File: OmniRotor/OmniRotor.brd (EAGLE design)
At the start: 118 parts, among them CON1 SPI, CON2 Telem, CON3 I2C, CON4 ADC, CON5 RC_IN, CON6 GPS, Q1 12MHz, U1 MAG3110, U2 LPS331AP, U3 HMC5883L, U4 BMP180, U6 XOR, U7 STM32F405RG, U8 LP2985-3.3, U9 LP2985-3.3

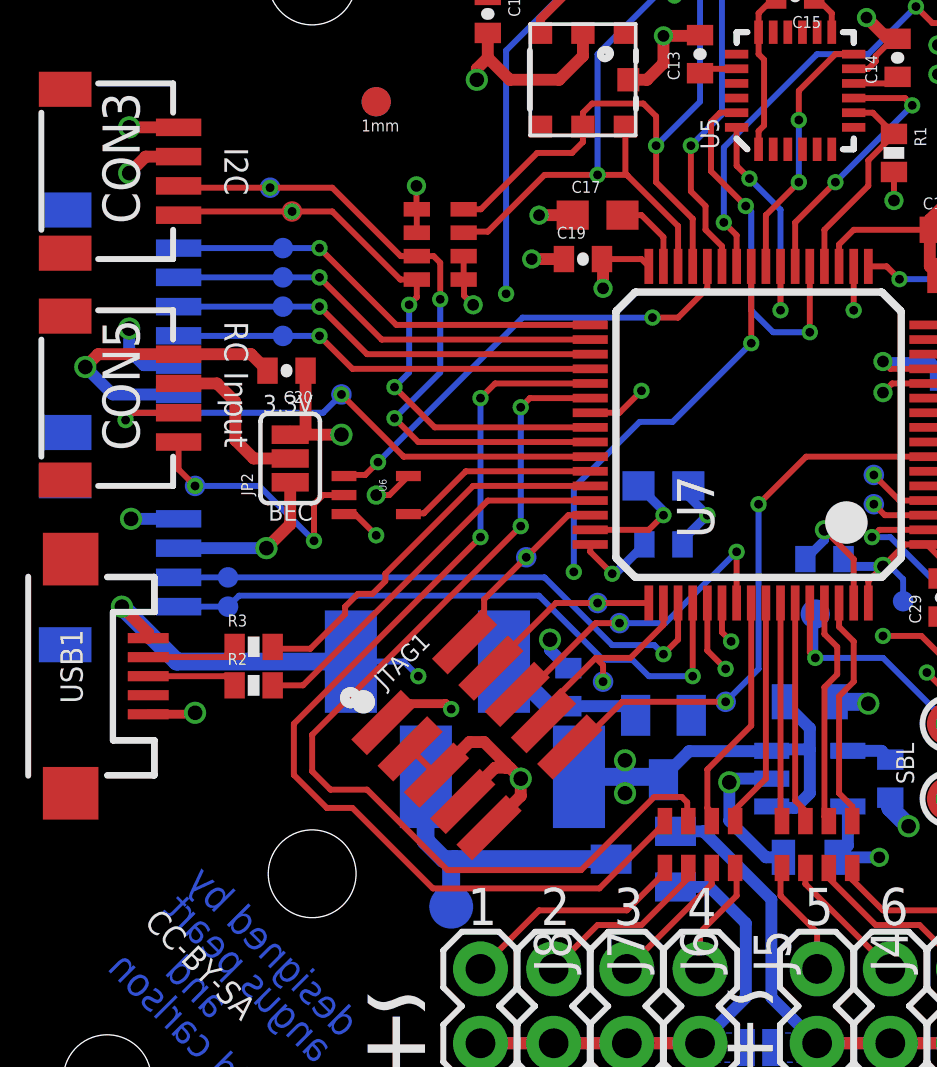
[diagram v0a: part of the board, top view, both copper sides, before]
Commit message: Changed debug interface from JTAG to SWD.
Frees up 2 GPIO. Also added pull-up and decoupling cap to reset line.
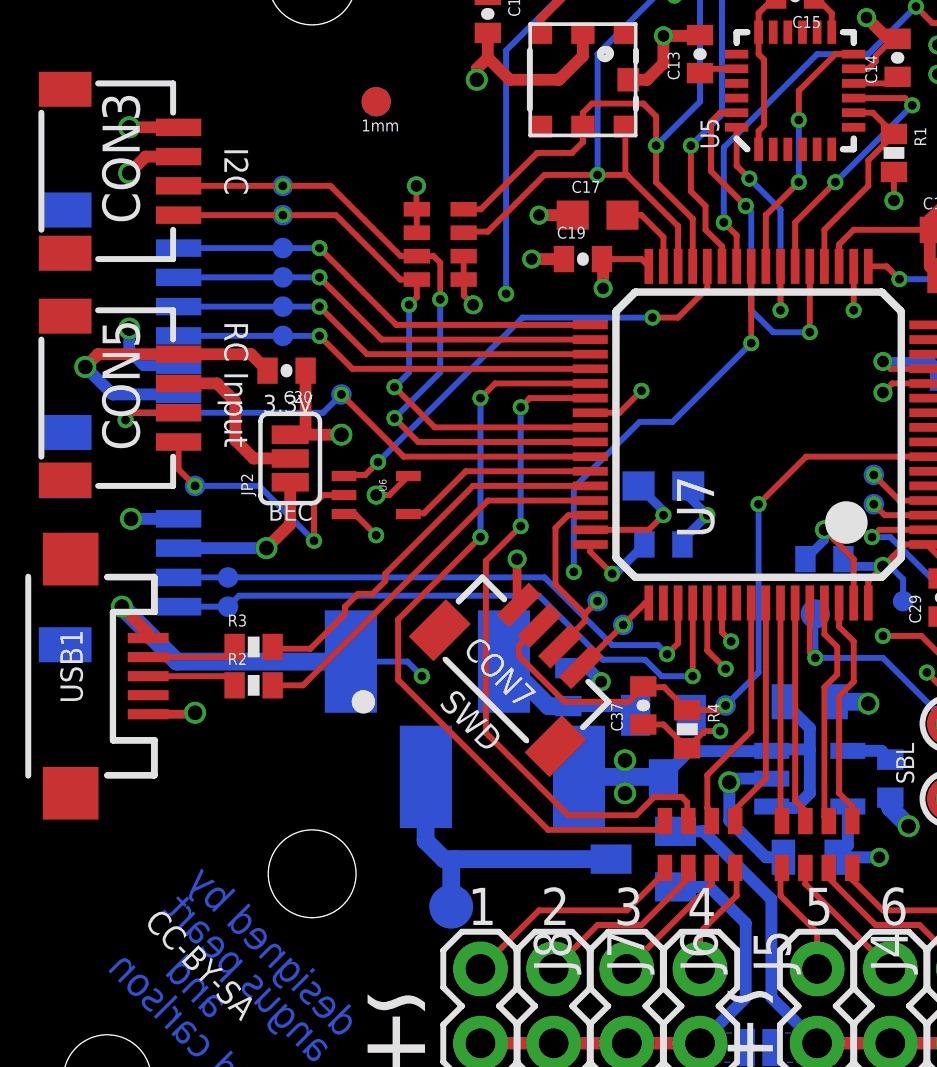
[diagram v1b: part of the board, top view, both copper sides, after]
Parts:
- removed JTAG1: (no value), OmniLoco:2X05-0.05IN
- removed TP21: TDO, OmniLoco:TESTPOINT_ROUND_0.7MM
- removed TP22: TDI, OmniLoco:TESTPOINT_ROUND_0.7MM
- added C37: 100nF, OmniLoco:0402-CAP
- added CON7: SWD, OmniLoco:BM04B-SRSS-TB
- added R4: 10K, OmniLoco:0402-RES
- TP19: value TMS -> SWDIO
- TP20: value TCLK -> SWDCLK
- TP23: value RST -> NRST
- moved TP19 2.86 mm to (19.5, 19.1)
- moved TP20 1.15 mm to (20.4, 18.2)
- moved TP9 0.44 mm to (8.75, 33.2)
- moved TP10 0.34 mm to (8.75, 32.2), flipped to the bottom
- moved TP23 0.12 mm to (23.9, 15.5)
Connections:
- removed net RST: JTAG1.10, TP23.1, U7.7
- removed net TCLK: JTAG1.4, TP20.1, U7.49
- removed net TDI: JTAG1.8, TP22.1, U7.50
- removed net TDO: JTAG1.6, TP21.1, U7.55
- removed net TMS: JTAG1.2, TP19.1, U7.46
- new net NRST: C37.2, CON7.2, R4.1, TP23.1, U7.7
- new net SWDCLK: CON7.4, TP20.1, U7.49
- new net SWDIO: CON7.3, TP19.1, U7.46
- net 3.3V: now also C37.1, R4.2; no longer JTAG1.1
- net GND: now also CON7.1; no longer JTAG1.3, JTAG1.5, JTAG1.7, JTAG1.9
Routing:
- net NRST: track 0.00 -> 23.5 mm, vias 0 -> 2
- net RST: track 19.6 -> 0.00 mm, vias 2 -> 0
- net TDO: track 11.3 -> 0.00 mm, vias 2 -> 0
- net N$50: track 33.9 -> 23.2 mm
- net N$49: track 34.8 -> 26.1 mm
- net GND: track 166.4 -> 158.6 mm
- net TDI: track 7.33 -> 0.00 mm, vias 1 -> 0
- net SWDIO: track 0.00 -> 6.90 mm, vias 0 -> 1
- net TMS: track 6.54 -> 0.00 mm, vias 1 -> 0
- net TCLK: track 6.32 -> 0.00 mm, vias 1 -> 0
- net SWDCLK: track 0.00 -> 3.22 mm, vias 0 -> 1
- net 3.3V: track 62.1 -> 62.6 mm
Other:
- board text added: "SWD"

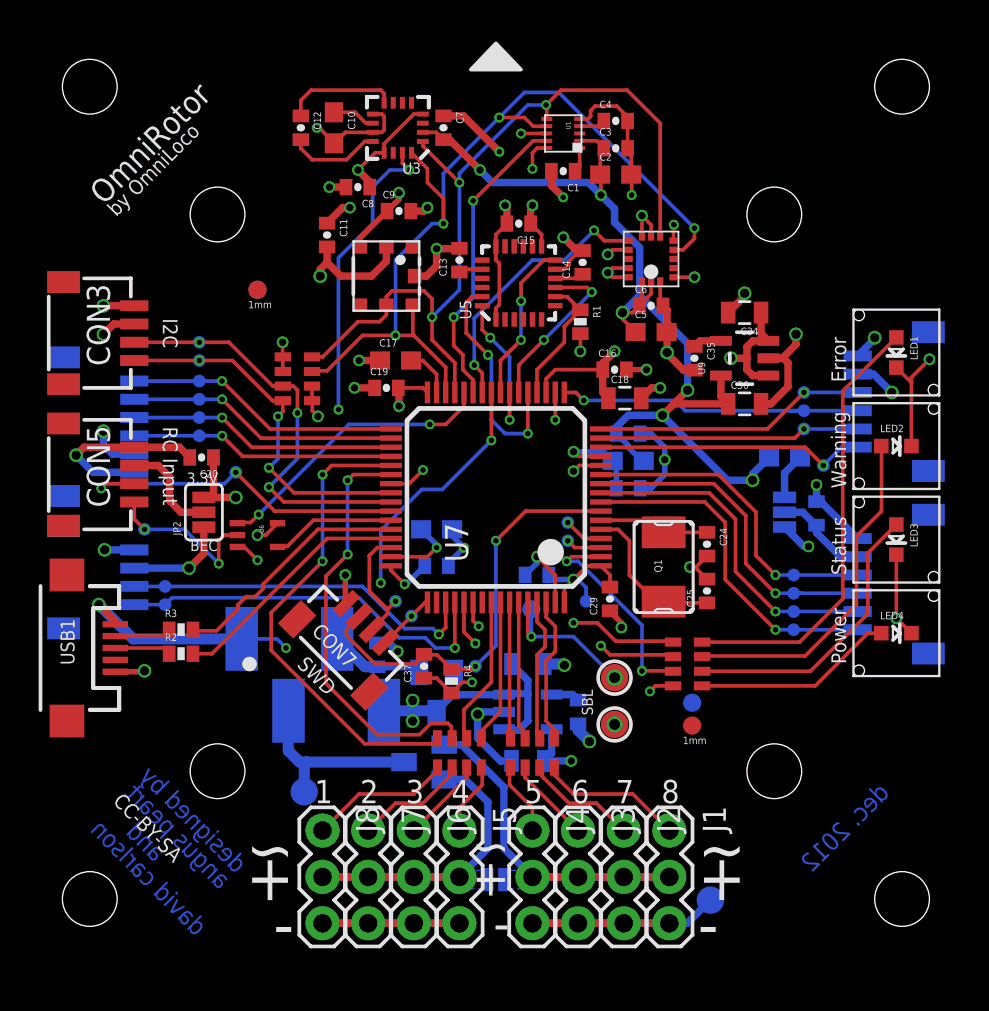
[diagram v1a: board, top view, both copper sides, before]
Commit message: More updates for Q4 2012 production.
- Added MS5611 pressure sensor
- Removed MAG3110
- Remapped some I/O pins
- Added additional UART connector
- Added Utility connector (PWM+ADC+SPI)
- Cleaned up all routing
- Moved magnetometer, fixed ground planes
- Changed PTC to 1210 package
- Re-aligned lightpipes
- Remapped most servo IO for maximum flexibility in other peripherals
- Replaced TX pin on RC Input connector with 3.3V, removed voltage
select jumper
- Changed crystal package and frequency
- Added 2.5x3.2mm crystal footprint
- Added lightpipe only footprint
- Removed lightpipe+LED conbimed footprint
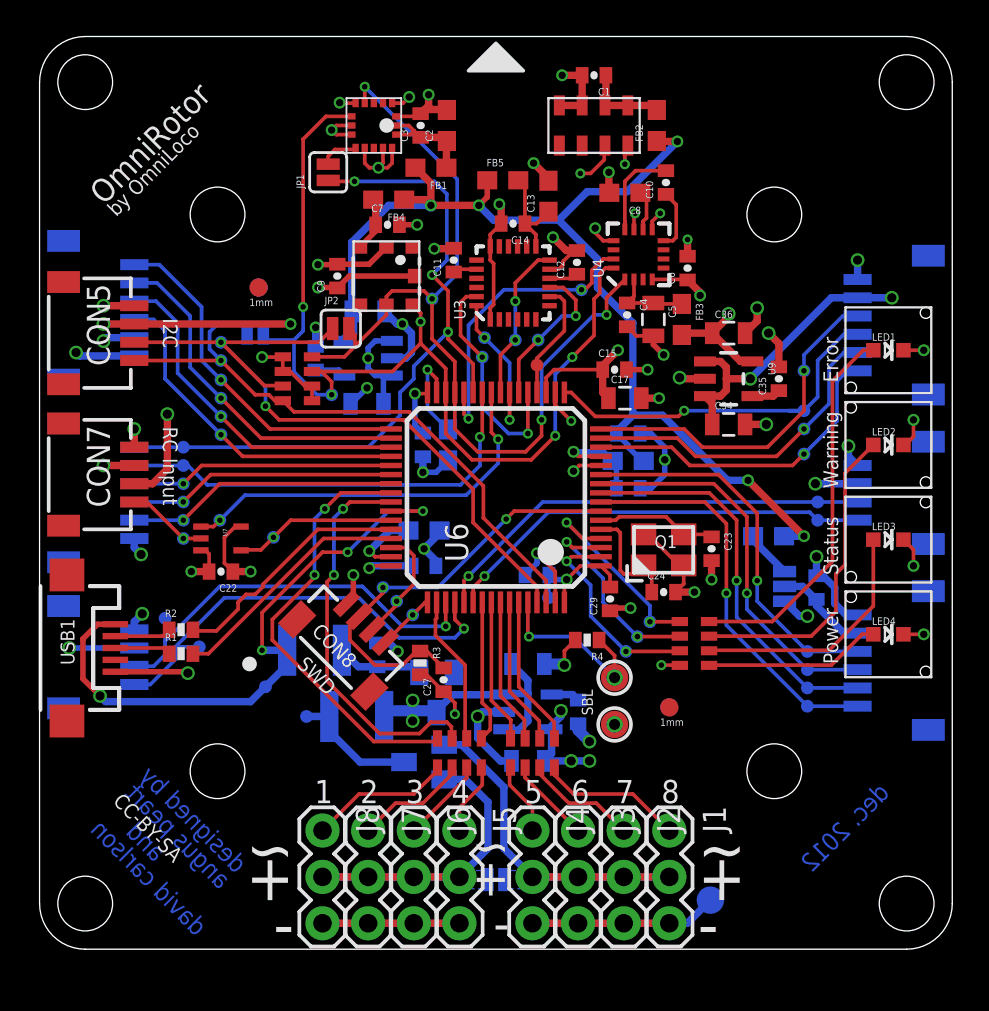
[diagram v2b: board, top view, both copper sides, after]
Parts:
- added C38: 100nF, OmniLoco:0402-CAP
- added C39: 10uF, OmniLoco:0805
- added CON8: SWD, OmniLoco:BM04B-SRSS-TB
- added CON9: GPS, OmniLoco:SM04B-SRSS-TB
- added FB3, FB4, FB5, FB6, FB7: 300mA, OmniLoco:0603
- added JP4: (no value), OmniLoco:SJ_3_PASTE1&2
- added JP5: BEC_JOIN, OmniLoco:SJ_2_NO
- added LP1, LP2, LP3, LP4: LIGHTPIPE, OmniLoco:VLP-LIGHTPIPES
- added TP21: CH13, OmniLoco:TESTPOINT_ROUND_0.7MM
- added TP22: SCL, OmniLoco:TESTPOINT_ROUND_0.7MM
- added TP33: P22, OmniLoco:TESTPOINT_ROUND_0.7MM
- added TP34: SWDCLK, OmniLoco:TESTPOINT_ROUND_0.7MM
- added TP35: SWDIO, OmniLoco:TESTPOINT_ROUND_0.7MM
- added TP36: NRST, OmniLoco:TESTPOINT_ROUND_0.7MM
- added TP37: SBL, OmniLoco:TESTPOINT_ROUND_1MM
- added TP38: SBL, OmniLoco:TESTPOINT_ROUND_1.5MM
- added TP39: 3.3V, OmniLoco:TESTPOINT_ROUND_1.5MM
- added TP40: GPS_TX, OmniLoco:TESTPOINT_ROUND_0.7MM
- added TP41: GPS_RX, OmniLoco:TESTPOINT_ROUND_0.7MM
- added TP42: BEC_IN, OmniLoco:TESTPOINT_ROUND_0.7MM
- added TP43: 3.3V, OmniLoco:TESTPOINT_ROUND_0.7MM
- added TP44: 3.3V-MAG, OmniLoco:TESTPOINT_ROUND_0.7MM
- added TP45: 3.3VA, OmniLoco:TESTPOINT_ROUND_0.7MM
- added TP46: PC13, OmniLoco:TESTPOINT_ROUND_0.7MM
- added TP47: PC14, OmniLoco:TESTPOINT_ROUND_0.7MM
- added TP48: PC15, OmniLoco:TESTPOINT_ROUND_0.7MM
- added TP49: GND, OmniLoco:TESTPOINT_ROUND_1.5MM
- added U10: LP2985-3.3 (MCP1801T-3302I), OmniLoco:SOT-23-5
- C10: value 4.7uF -> 220nF; device OmniLoco:0603 -> OmniLoco:0402-CAP
- C11: value 100nF -> 2.2nF (50v)
- C12: value 220nF -> 100nF
- C13: value 2.2nF (50v) -> 1uF; device OmniLoco:0402-CAP -> OmniLoco:0603
- C16: value 100nF -> 2.2uF; device OmniLoco:0402-CAP -> OmniLoco:0603
- C17: value 2.2uF -> 10uF; device OmniLoco:0603 -> OmniLoco:0805
- C18: value 10uF -> 100nF; device OmniLoco:0805 -> OmniLoco:0402-CAP
- C19: value 100nF -> 10nF
- C2: value 1uF -> 10uF?
- C21: value 10nF -> 100nF
- C23: value 100nF -> 8pF
- C25: value 8pF -> 2.2uF; device OmniLoco:0402-CAP -> OmniLoco:0603
- C26: value 2.2uF -> 100nF; device OmniLoco:0603 -> OmniLoco:0402-CAP
- C37: value 100nF -> 10uF; device OmniLoco:0402-CAP -> OmniLoco:0805
- C5: value 10uF? -> 10uF; device OmniLoco:0603 -> OmniLoco:0805
- C8: value 100nF -> 4.7uF; device OmniLoco:0402-CAP -> OmniLoco:0603
- CON1: value SPI -> Telem
- CON2: value Telem -> SPI
- CON3: value I2C -> Utility; device OmniLoco:SM04B-SRSS-TB -> OmniLoco:SM06B-SRSS-TB
- CON4: value ADC -> I2C; device OmniLoco:SM06B-SRSS-TB -> OmniLoco:SM04B-SRSS-TB
- CON5: value RC_IN -> I2C
- CON6: value GPS -> ADC; device OmniLoco:SM04B-SRSS-TB -> OmniLoco:SM06B-SRSS-TB
- CON7: value SWD -> RC_IN; device OmniLoco:BM04B-SRSS-TB -> OmniLoco:SM04B-SRSS-TB
- F1, F2: device OmniLoco:1812 -> OmniLoco:1210-PTC
- JP1: value (none) -> PB1; device OmniLoco:SJ_3_PASTE1&2 -> OmniLoco:SJ_2_NO
- JP2: value (none) -> PB1; device OmniLoco:SJ_3_PASTE2&3 -> OmniLoco:SJ_2_NO
- JP3: value BEC_JOIN -> PB1
- LED1, LED2, LED3, LED4: device OmniLoco:0603_LED_VLPXXX_LIGHTPIPES -> OmniLoco:0603_LED
- Q1: value 12MHz -> 16MHz; device OmniLoco:CRYSTAL-5X3-2 -> OmniLoco:XTAL_3-2X3-5
- R1: value 10K -> 22R
- R3: value 22R -> 10K
- TP1: value MOSI -> MPU_INT
- TP10: value SDA -> TELEM_RX
- TP11: value RC_TX -> TELEM_RTS
- TP12: value RC_RX -> TELEM_CTS
- TP13: value PC15 -> MOSI
- TP14: value PC14 -> MISO
- TP15: value ADC0 -> SCK
- TP16: value ADC1 -> CS
- TP17: value ADC2 -> CH9
- TP18: value ADC3 -> CH10
- TP19: value SWDIO -> CH11
- TP2: value MISO -> MPU_MISO
- TP20: value SWDCLK -> CH12
- TP23: value NRST -> SDA
- TP24: value GPS_TX -> RX_INV
- TP25: value BEC_IN -> RC_RX; device OmniLoco:TESTPOINT_ROUND_1.5MM -> OmniLoco:TESTPOINT_ROUND_0.7MM
- TP26: value GPS_RX -> RX_XOR
- TP27: value SBL -> ADC0; device OmniLoco:TESTPOINT_ROUND_1MM -> OmniLoco:TESTPOINT_ROUND_0.7MM
- TP28: value SBL -> ADC1; device OmniLoco:TESTPOINT_ROUND_1.5MM -> OmniLoco:TESTPOINT_ROUND_0.7MM
- TP29: value 3.3V -> ADC2; device OmniLoco:TESTPOINT_ROUND_1.5MM -> OmniLoco:TESTPOINT_ROUND_0.7MM
- TP3: value SCK -> MPU_CS
- TP30: value 3.3V -> ADC3
- TP31: value 3.3VA -> VBUS
- TP32: value GND -> PC12; device OmniLoco:TESTPOINT_ROUND_1.5MM -> OmniLoco:TESTPOINT_ROUND_0.7MM
- TP4: value CS -> MPU_MOSI
- TP5: value TELEM_TX -> MPU_SCK
- TP6: value TELEM_RX -> SDA
- TP7: value TELEM_RTS -> SCL
- TP8: value TELEM_CTS -> MAG_DRDY
- TP9: value SCL -> TELEM_TX
- U1: value MAG3110 -> MS5611-B03; device OmniLoco:DFN-10 -> OmniLoco:MS5611
- U3: value HMC5883L -> (none); device OmniLoco:16LPCC -> OmniLoco:QFN-24
- U4: value BMP180 -> HMC5883L; device OmniLoco:BMP180 -> OmniLoco:16LPCC
- U5: value (none) -> BMP180; device OmniLoco:QFN-24 -> OmniLoco:BMP180
- U6: value XOR -> STM32F405RG; device OmniLoco:SC-70-5 -> OmniLoco:LQFP64
- U7: value STM32F405RG -> XOR; device OmniLoco:LQFP64 -> OmniLoco:SC-70-5
- U8: value LP2985-3.3 -> LP2985-3.3 (MCP1802T-3302I)
- U9: value LP2985-3.3 -> LP2985-3.3 (MCP1801T-3302I)
- moved CON1 41.0 mm to (44.8, 36.7), turned to 270 degrees
- moved CON6 39.6 mm to (44.8, 18.3), turned to 270 degrees
- moved CON2 39.6 mm to (5.19, 32.5), turned to 90 degrees
- moved TP12 36.4 mm to (41.9, 27.1)
- moved TP18 34.2 mm to (7.88, 24.5)
- moved TP17 33.8 mm to (7.88, 23.5)
- moved TP16 33.5 mm to (9.94, 31.2)
- moved TP10 33.2 mm to (41.9, 29.5)
- moved TP9 33.2 mm to (41.9, 31.7)
- moved TP15 32.8 mm to (9.94, 30.2)
- moved JP3 32.7 mm to (11.8, 33.8), turned to 180 degrees
- moved TP11 31.2 mm to (41.9, 28.5)
- moved JP1 31.2 mm to (15.8, 42.6), flipped to the top
- moved R1 28.4 mm to (7.75, 16.2), turned to 0 degrees
- moved TP31 26.4 mm to (12.4, 14.4)
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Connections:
- removed net N$12: C1.1, U1.1
- removed net N$14: U6.1, U7.28
- removed net N$17: R1.1, U5.8, U7.20
- removed net N$19: TP13.1, U7.4
- removed net N$22: U5.24, U7.23
- removed net N$25: U5.9, U7.22
- removed net N$27: U5.23, U7.21
- removed net N$28: U5.12, U7.24
- removed net N$42: RA2.D1, U7.58
- removed net N$43: RA2.C1, U7.59
- removed net N$45: RA2.A1, U7.62
- removed net N$47: RA3.A1, U7.57
- removed net N$48: RA3.B1, U7.56
- removed net N$49: RA3.D1, U7.37
- removed net N$50: RA3.C1, U7.38
- removed net N$55: RA4.B1, U7.53
- removed net N$56: RA4.A1, U7.54
- removed net N$57: RA4.C1, U7.2
- removed net N$59: C4.1, U1.4
- removed net RC_TX: CON5.3, TP11.1, U7.42
- new net 3.3V-MAG: C36.1, FB3.2, TP44.1, U9.5
- new net MAG_DRDY: TP8.1, U4.15, U6.28
- new net MPU_CS: TP3.1, U3.8, U6.20
- new net MPU_INT: TP1.1, U3.12, U6.24
- new net MPU_MISO: TP2.1, U3.9, U6.22
- new net MPU_MOSI: TP4.1, U3.24, U6.23
- new net MPU_SCK: TP5.1, U3.23, U6.21
- new net N$51: C38.1, U10.4
- new net N$54: C4.1, C5.1, FB3.1, U4.2
- new net N$58: C7.1, FB4.2, U5.3
- new net N$64: C1.1, FB2.2, U1.1, U1.2
- new net PA15: RA3.D1, U6.40
- new net PB3: RA3.C1, U6.41
- new net PB4: RA3.B1, U6.50
- new net PB5: RA3.A1, U6.55
- new net PB6: RA2.D1, U6.56
- new net PB7: RA2.C1, U6.57
- new net PB8: RA2.B1, U6.58
- new net PB9: RA2.A1, U6.59
- new net PC13: RA4.C1, TP46.1, U6.2
- new net PC14: RA4.B1, TP47.1, U6.3
- new net PC15: RA4.A1, TP48.1, U6.4
- new net PC6: CON3.4, TP19.1, U6.37
- new net PC7: CON3.3, TP18.1, U6.38
- new net PC8: CON3.2, TP17.1, U6.39
- new net USART5_RX: CON4.4, TP33.1, U6.54
- new net USART5_TX: CON4.3, TP32.1, U6.53
- net 3.3V: now also C17.1, C18.2, C22.1, C26.1, C6.1, C9.2, CON4.2, CON7.3, JP4.1, R3.2, TP39.1, TP43.1, U4.13, U4.4, U5.2, U6.1, U6.19, U6.32, U6.48, U6.64, U7.5; no longer C11.2, C16.1, C18.1, C19.2, C20.1, C37.1, C8.1, JP1.1, JP2.3, R1.2, R4.2, TP29.1, TP30.1, U1.8, U3.13, U3.4, U4.2, U5.13, U6.5, U7.1, U7.19, U7.32, U7.48, U7.64
- net 3.3VA: now also C20.1, C39.1, FB2.1, FB4.1, FB5.1, FB6.2, FB7.2, TP45.1, U10.5; no longer C2.1, C22.1, C3.1, C36.1, C5.1, C6.1, C7.2, C9.1, FB2.2, TP31.1, U1.2, U2.14, U2.15, U3.2, U4.3, U9.5
- net ADC0: now also CON6.3, TP27.1, U6.11; no longer CON4.3, TP15.1, U7.11
- net ADC1: now also CON6.4, TP28.1, U6.10; no longer CON4.4, TP16.1, U7.10
- net ADC2: now also CON6.5, TP29.1, U6.9; no longer CON4.5, TP17.1, U7.9
- net ADC3: now also CON6.6, TP30.1, U6.8; no longer CON4.6, TP18.1, U7.8
- net BEC1: now also JP5.1; no longer JP3.1
- net BEC2: now also JP5.2; no longer JP3.2
- net BEC_IN: now also TP42.1; no longer TP25.1
- net CS: now also CON2.6, TP16.1, U6.33; no longer CON1.6, TP4.1, U7.33
- net GND: now also C11.2, C12.2, C16.1, C17.2, C18.1, C19.2, C37.2, C38.2, C39.2, C7.2, C9.1, CON6.1, CON8.1, CON9.4, Q1.2, Q1.4, R4.2, TP49.1, U1.3, U1.4, U10.2, U3.1, U3.18, U4.11, U4.9, U5.7, U6.12, U6.18, U6.63, U7.3; no longer C10.2, C11.1, C16.2, C17.1, C18.2, C19.1, C27.2, C7.1, C9.2, CON6.4, TP32.1, U1.10, U1.5, U3.9, U4.7, U5.1, U5.11, U5.18, U6.3, U7.12, U7.18, U7.63
- net GPS_TX: now also CON9.2, TP40.1, U6.51; no longer CON6.2, TP24.1, U7.51
- net GPX_RX: now also CON9.1, TP41.1, U6.52; no longer CON6.1, TP26.1, U7.52
- net MISO: now also CON2.4, TP14.1, U6.35; no longer CON1.4, TP2.1, U7.35
- net MOSI: now also CON2.3, TP13.1, U6.36; no longer CON1.3, TP1.1, U7.36
- net N$1: now also C19.1, FB7.1, U6.13; no longer C21.1, FB2.1, U7.13
- net N$10: now also R2.2, U6.44; no longer R3.2, U7.44
- net N$11: now also R1.2, U6.45; no longer R2.2, U7.45
- net N$13: now also TP26.1, U6.43, U7.4; no longer U6.4, U7.43
- net N$15: now also C10.1, U4.8; no longer C12.1, U3.8
- net N$16: now also C10.2, U4.12; no longer C12.2, U3.12
- net N$18: now also C13.1, C14.1, FB5.2, U3.13; no longer U3.15, U7.39
- net N$2: now also C23.1, Q1.3, U6.6; no longer C24.1, Q1.2, U7.6
- net N$20: now also C8.1, U4.10; no longer C10.1, U3.10
- net N$21: now also C21.1, CON6.2, JP4.2; no longer C23.1, CON4.2, JP1.2
- net N$23: now also C2.1, C3.1, FB1.1, U2.14, U2.15; no longer TP14.1, U7.3
- net N$29: now also FB6.1, JP4.3; no longer FB1.1, JP1.3
- net N$3: now also C24.1, U6.5; no longer C25.1, U7.5
- net N$31: now also C11.1, U3.20; no longer C13.1, U5.20
- net N$32: now also C12.1, U3.10; no longer C14.1, U5.10
- net N$44: now also JP1.2, U2.9; no longer RA2.B1, U7.61
- net N$46: now also R4.1, TP37.1, TP38.1, U6.60; no longer TP27.1, TP28.1, U7.60
- net N$6: now also TP24.1, U6.25, U7.1; no longer CON5.2, JP2.2
- net N$8: now also R1.1; no longer R2.1
- net N$9: now also R2.1; no longer R3.1
- net NRST: now also C27.2, CON8.2, R3.1, TP36.1, U6.7; no longer C37.2, CON7.2, R4.1, TP23.1, U7.7
- net PB0: now also CON3.5, TP20.1, U6.26; no longer U2.9, U7.26
- net PB1: now also CON3.6, JP1.1, TP21.1, U6.27; no longer U1.9, U7.27
- net RC_RX: now also CON7.4, TP25.1, U7.2; no longer CON5.4, TP12.1, U6.2
- net SCK: now also CON2.5, TP15.1, U6.34; no longer CON1.5, TP3.1, U7.34
- net SCL: now also JP2.2, RA1.A2, TP7.1, U1.8, U4.1, U5.5, U6.29; no longer RA1.B2, U1.7, U3.16, U4.6, U7.30
- net SCL-EXT: now also CON5.3, JP2.1, TP22.1, U6.61; no longer CON3.3, TP9.1, U7.41
- net SDA: now also JP3.2, RA1.B2, TP6.1, U1.7, U4.16, U5.6, U6.30; no longer RA1.A2, U1.6, U3.1, U4.5, U7.29
- net SDA-EXT: now also CON5.4, JP3.1, TP23.1, U6.62; no longer CON3.4, TP10.1, U7.40
- net SWDCLK: now also CON8.4, TP34.1, U6.49; no longer CON7.4, TP20.1, U7.49
- net SWDIO: now also CON8.3, TP35.1, U6.46; no longer CON7.3, TP19.1, U7.46
- net TELEM_CTS: now also CON1.6, TP12.1, U6.14; no longer CON2.6, TP8.1, U7.14
- net TELEM_RTS: now also CON1.5, TP11.1, U6.15; no longer CON2.5, TP7.1, U7.15
- net TELEM_RX: now also CON1.4, TP10.1, U6.17; no longer CON2.4, TP6.1, U7.17
- net TELEM_TX: now also CON1.3, TP9.1, U6.16; no longer CON2.3, TP5.1, U7.16
- net VCAP@1: now also C16.2, U6.31; no longer C17.2, U7.31
- net VCAP@2: now also C25.1, U6.47; no longer C26.1, U7.47
- net VCC: now also C37.1, CON5.2, CON7.2, CON9.3, U10.1, U10.3; no longer CON3.2, CON6.3, JP2.1
- net VUSB: now also TP31.1, U6.42; no longer U7.25
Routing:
- net VCC: track 123.4 -> 153.5 mm, vias 7 -> 10
- net N$49: track 26.1 -> 0.00 mm, vias 2 -> 0
- net USART5_TX: track 0.00 -> 24.5 mm, vias 0 -> 1
- net PA15: track 0.00 -> 23.8 mm, vias 0 -> 2
- net USART5_RX: track 0.00 -> 23.8 mm, vias 0 -> 1
- net N$50: track 23.2 -> 0.00 mm, vias 2 -> 0
- net PB1: track 16.8 -> 39.9 mm, vias 2 -> 3
- net PB3: track 0.00 -> 21.6 mm, vias 0 -> 2
- net SDA: track 46.7 -> 67.6 mm, vias 3 -> 6
- net RC_TX: track 19.0 -> 0.00 mm, vias 2 -> 0
- net N$18: track 24.5 -> 5.58 mm, vias 3 -> 0
- net SCL-EXT: track 23.0 -> 41.0 mm, vias 3 -> 2
- net MAG_DRDY: track 0.00 -> 16.5 mm, vias 0 -> 2
- net N$6: track 5.64 -> 21.8 mm, vias 0 -> 2
- net N$14: track 15.8 -> 0.00 mm, vias 2 -> 0
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- added copper zone on layer 15, net N$60
- added copper zone on layer 2, net N$61
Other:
- board outline added: 50 x 50 mm
- board text added: "Analogs"
- board text added: "Serial"
- board text added: "Utility"
- board text removed: "ADC+IO"

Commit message: Board functional design done, silkscreen updated
- Board routing and pin re-mapping complete
- Started on silkscreen changes
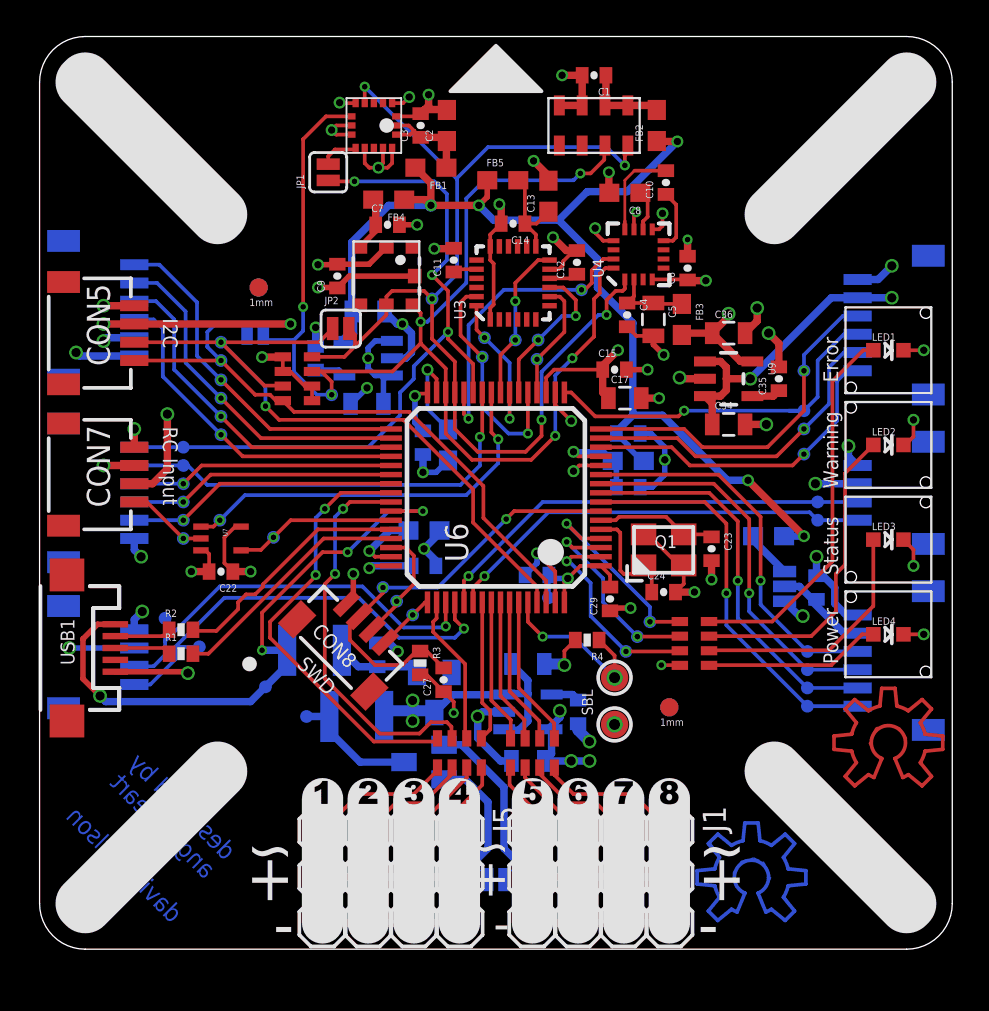
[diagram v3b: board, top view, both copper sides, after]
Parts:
- removed TP49: GND, OmniLoco:TESTPOINT_ROUND_1.5MM
- added U$16: (no value), OmniLoco:SILK-SERVO-1
- added U$24: (no value), OmniLoco:SILK-SERVO-4
- added U$28: (no value), OmniLoco:SILK-SERVO-3
- added U$31: (no value), OmniLoco:SILK-SERVO-2
- added U$32: (no value), OmniLoco:SILK-SERVO-5
- added U$33: (no value), OmniLoco:SILK-SERVO-6
- added U$34: (no value), OmniLoco:SILK-SERVO-7
- added U$35: (no value), OmniLoco:SILK-SERVO-8
- Q1: device OmniLoco:XTAL_3-2X3-5 -> OmniLoco:CRYSTAL_3-2X2-5
- moved TP3 0.31 mm to (27.2, 32.3), flipped to the bottom
- moved C18 0.12 mm to (21.0, 27.8)
- moved D1 0.12 mm to (21.6, 14.1)
- moved C19 0.06 mm to (32.2, 25.3)
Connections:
- net GND: no longer TP49.1
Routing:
- net N$14: track 0.00 -> 28.4 mm
- net N$12: track 0.00 -> 28.4 mm
- net SDA: track 67.6 -> 71.8 mm
- net GND: track 153.0 -> 152.2 mm
- net SCL: track 60.2 -> 60.9 mm
- net 3.3V: track 61.0 -> 60.3 mm
- net MPU_CS: vias 0 -> 1
- added copper zone on layer 1, net N$12
- added copper zone on layer 16, net N$14
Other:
- board text added: "designed by angus peart and david carlson"
- board text removed: "1"
- board text removed: "2"
- board text removed: "3"
- board text removed: "4"
- board text removed: "5"
- board text removed: "6"
- board text removed: "7"
- board text removed: "8"
- board text removed: "BEC"
- board text removed: "CC-BY-SA"
- board text removed: "JOIN"
- board text removed: "OmniRotor"
- board text removed: "and"
- board text removed: "angus peart"
- board text removed: "by OmniLoco"
- board text removed: "david carlson"
- board text removed: "designed by"
